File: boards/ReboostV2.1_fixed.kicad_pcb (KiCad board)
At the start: 4 copper layers, 94.5 x 80.5 mm, 184 parts, among them J1 Header 1x4, J2 USB-B-MINI-VERT, J4 TagConnect 6p NL, J8 CAN_BUS-Deutsch_ASL206-05SD-HE, J9 CAN_BUS-Deutsch_ASL206-05SD-HE, Q1 GS61008T, Q2 GS61008T, Q3 MMBT5401LT1G, U10 LP2985AIM5-3.3, U11 TPS7A2501, U1_IHS LTC6362, U1_ILS LTC6362, U2 CP2104-F03-GM, U3 STM32G474, U4 74LVC2G08, U5 Si8273, U6 ISO1044, U7 LM5165XDRCT, U8 LTC3639EMSE, U9 LM5165YDRCT, X1 16MHz

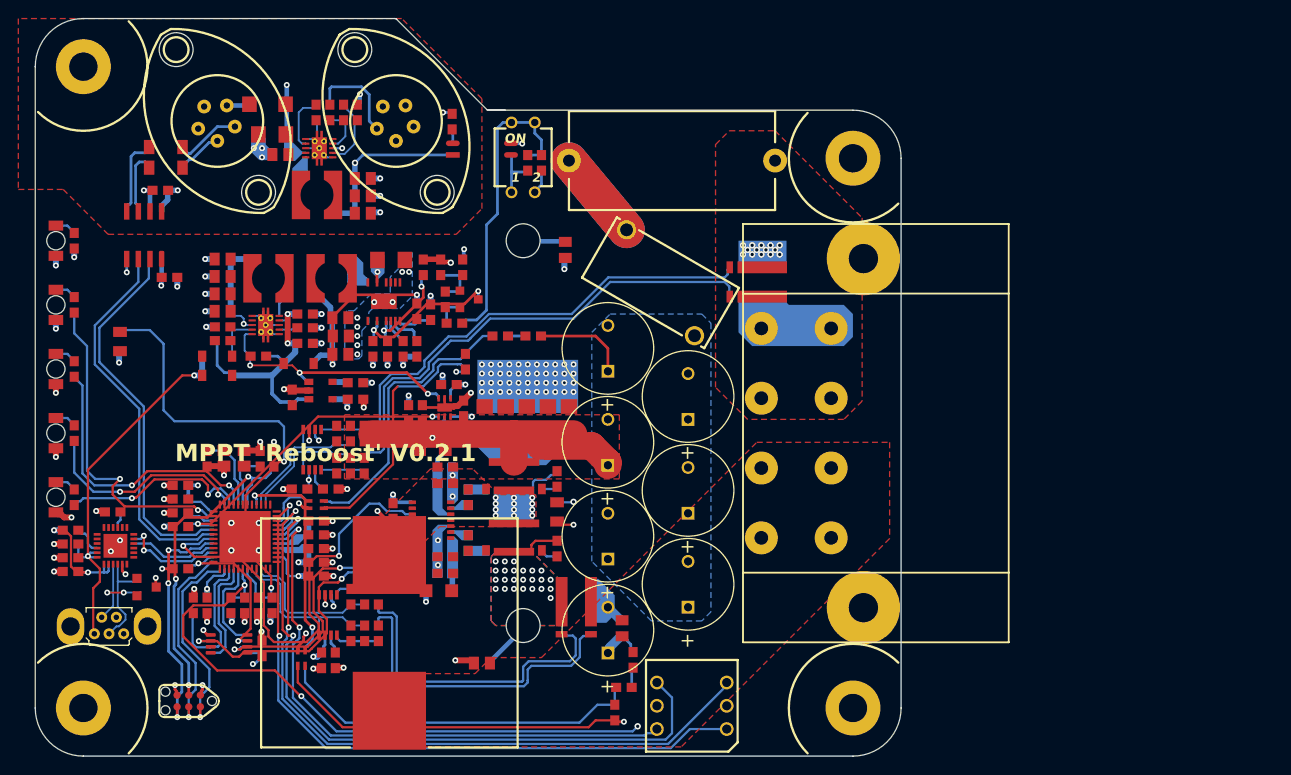
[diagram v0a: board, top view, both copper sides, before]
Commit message: boards: regenerate ReboostV2.1_fixed with faithful relayer (correct full-board layers)
Was the partial-relayer conversion (pads+power on F.Cu, signal traces stranded on
B.Cu, 160/184 footprints on the wrong side). Regenerated with --relayer faithful:
footprints 160 front / 24 back, tracks Top 1184 / Bottom 167 / In2 82 / In1 3 (=
the Altium copper histogram through LMAP), MCU/Q1/Q2 front with pads+traces on
matching layers. 1436 tracks relayered, 184 footprints flipped, 18 zones swapped.
Adds the .altium.json conversion provenance sidecar.
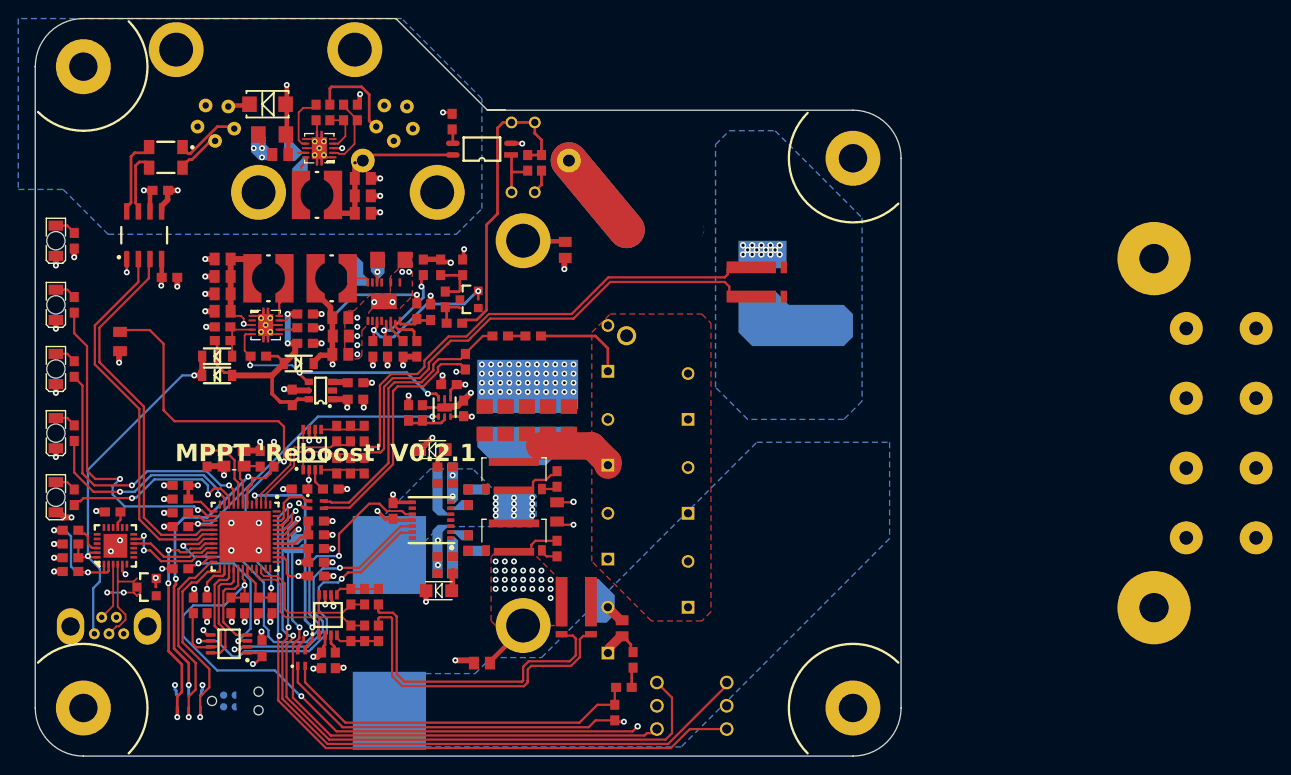
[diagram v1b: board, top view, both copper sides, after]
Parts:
- ? (x7), C22, C23, C24, C25, C26, C28, C34, F1, J1, J2, J4, J8, J9, L1, L2, S1, S2: moved to B.Cu
- C10, C11, C12, C13, C14, C15, C16, C17, C18, C19, C1_IHS, C1_ILS, C20, C21, C27, C29, C2_IHS, C2_ILS, C30, C31, C32, C33, C35, C36, C37, C38, C39, C3_IHS, C3_ILS, C40, C41, C42, C43, C44, C45, C46, C47, C48, C49, C4_IHS, C4_ILS, C5, C50, C51, C52, C53, C54, C55, C56, C57, C58, C59, C6, C60, C61, C62, C64, C65, C66, C67, C7, C8, C9, D1, D2, D3, D4, D5, D6, D7, D8, L3, L4, L5, L6, L7_VHS, L7_VLS, LED1, LED2, LED3, LED4, LED5, MP1, MP2, MP3, MP4, MP5, MP6, Q1, Q2, Q3, R1, R10_IHS, R10_ILS, R11, R12_VHS, R12_VLS, R13_VHS, R13_VLS, R14, R15, R16, R17, R18, R19, R2, R20, R21, R22, R24, R25, R26, R27, R28, R29, R3, R30, R31, R32, R33, R34, R35, R36, R37, R38, R39, R4, R40, R41, R42, R44, R45, R47, R48, R49_VHS, R49_VLS, R5, R50, R53, R6_IHS, R6_ILS, R7_IHS, R7_ILS, R8_IHS, R8_ILS, R9_IHS, R9_ILS, U10, U11, U1_IHS, U1_ILS, U2, U3, U4, U5, U6, U7, U8, U9, X1: moved to F.Cu
- turned ? to 180 degrees (x7)
- turned C12 to 0 degrees
- turned C14 to 0 degrees
- turned C15 to 0 degrees
- turned C17 to 180 degrees
- turned C18 to 0 degrees
- turned C19 to 180 degrees
- turned C27 to 180 degrees
- turned C2_IHS to 180 degrees
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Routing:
- net VLP: track 43.9 -> 4.08 mm, vias 1 -> 0
- net GND: track 125.4 -> 160.7 mm, vias 161 -> 132
- net NetC14_2: track 5.34 -> 32.8 mm, vias 0 -> 5
- net SWO: track 25.6 -> 0.00 mm, vias 3 -> 0
- net Vb: track 87.6 -> 62.6 mm
- net Vdda: track 16.5 -> 29.5 mm, vias 6 -> 10
- net RX: track 9.69 -> 0.00 mm
- net LS: track 10.3 -> 1.06 mm, vias 0 -> 1
- net VDD_CP: track 13.5 -> 19.1 mm, vias 2 -> 4
- net HSS: track 21.6 -> 17.4 mm, vias 15 -> 14
- net NetC27_2: track 5.60 -> 2.20 mm, vias 0 -> 1
- net CGND: track 26.2 -> 22.9 mm, vias 9 -> 3
- net NetR11_1: track 3.33 -> 0.00 mm
- net 5Vcan: track 48.8 -> 51.9 mm, vias 3 -> 6
- net Vusb: track 42.5 -> 44.4 mm, vias 2 -> 4
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- added copper zone on In1.Cu, net CGND
- added copper zone on In1.Cu, net GND
- added copper zone on B.Cu, net HSS
- added copper zone on B.Cu, net SHLD
- added copper zone on B.Cu, net VHP
- added copper zone on In2.Cu, net VHP
- added copper zone on In2.Cu, net VLN
- added copper zone on B.Cu, net VLP
- added copper zone on In2.Cu, net Vdd
- added copper zone on In2.Cu, net Vdda
- removed copper zone on In2.Cu, net CGND
- removed copper zone on B.Cu, net GND
- removed copper zone on In2.Cu, net GND
- removed copper zone on F.Cu, net HSS
- removed copper zone on F.Cu, net SHLD
- removed copper zone on F.Cu, net VHP
- removed copper zone on In1.Cu, net VHP
- removed copper zone on In1.Cu, net VLN
- removed copper zone on F.Cu, net VLP
- removed copper zone on B.Cu, net Vb
- removed copper zone on In1.Cu, net Vdd
- removed copper zone on In1.Cu, net Vdda

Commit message: altium_import: relabel layers instead of mirroring footprints; restore the pour guard
The 'faithful' relayer used fp.Flip(fp.GetPosition(), False) on every footprint.
Flip() MIRRORS each footprint's pad offsets about its own anchor, while tracks
and zones were only layer-swapped, never mirrored -- so pads ended up on copper
they do not touch on the real board. Measured against the raw import, the
committed board had 355 of 544 pads displaced: MLCC terminals exchanged ends by
+-1.7 mm, and Q2's G1/G2 gate pads swapped places by +-6.1 mm.

We are re-interpreting which physical layer each object lives on, not moving
parts to the other side of the board, so the geometry must not move at all.
_relayer_faithful is now a pure layer relabel (pad layer-sets, footprint side
flag, tracks, arcs, blind/buried via spans, zones incl. footprint-owned ones,
and board-level copper shapes). Re-measured: 0 of 541 referenced pads move.

Two things that relabel was still missing, both silent:
  - PCB_ARC copper and board-level gr_* copper shapes were left on the
    un-relabelled layer. ReboostV2 has no arcs but 26 copper shapes -- they
    were stranded on the wrong layer in the committed board.
  - boards with copper beyond In2 were mis-relabelled (only F/B and In1/In2 are
    known); that now raises rather than producing a mixed stack.

The Vb-pour check had been narrowed to `relayer == "partial"`, so 'none',
'groundtruth' and 'faithful' lost BOTH the bridging pour and the warning that
the importer had dropped one. A dropped FET-area Vin pour breaks the loop
whichever relayer ran, so the CHECK is restored for every mode; only the
SYNTHESIS stays partial-only, and the others get a loud warning instead of
invented copper. It fires on the real board: the only surviving Vb zone spans
x=162..175 mm while Q1's Vb pad is at x=153.5 mm.

The check itself was also too weak. It tested a zone BOUNDING-BOX overlap of a
possibly-unfilled zone, so a ring/L-shaped pour elsewhere on the net, or a zon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
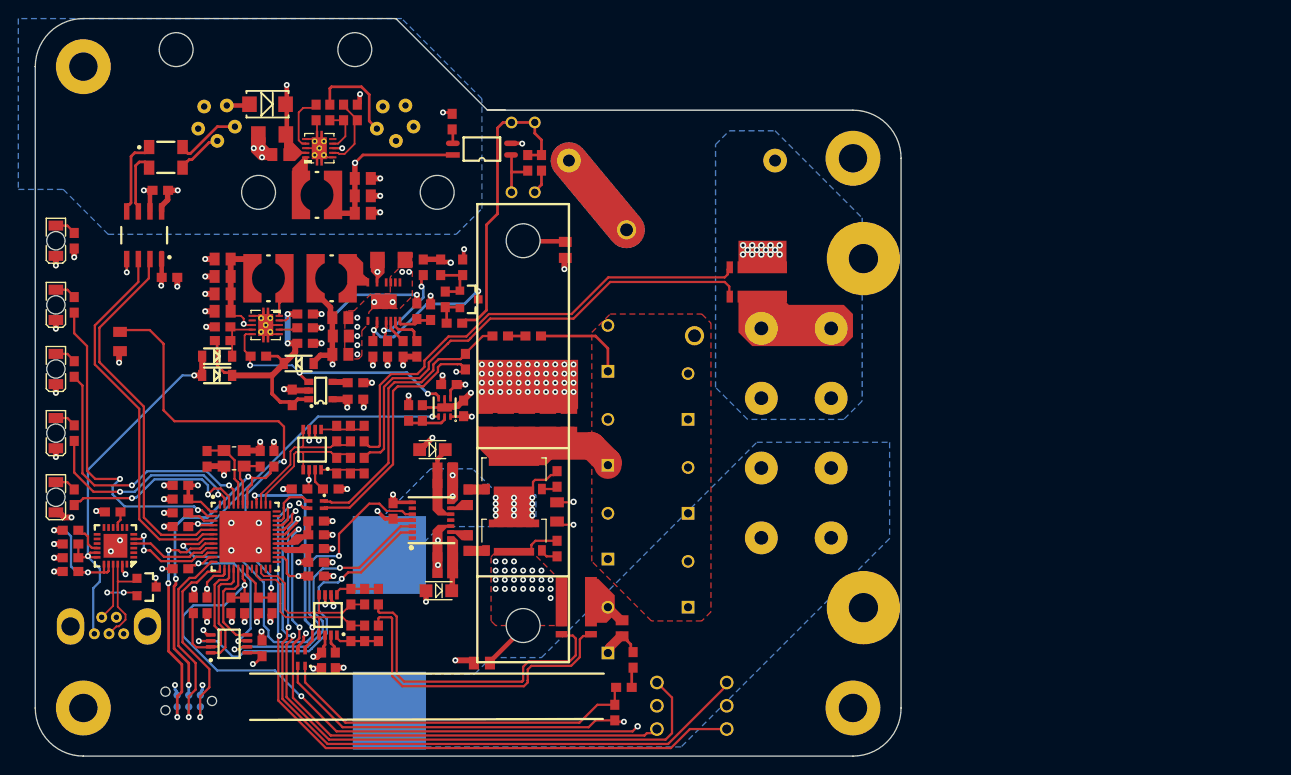
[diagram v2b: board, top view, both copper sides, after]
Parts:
- turned ? to 0 degrees (x7)
- turned C12 to 180 degrees
- turned C14 to 180 degrees
- turned C15 to 180 degrees
- turned C17 to 0 degrees
- turned C18 to 180 degrees
- turned C19 to 0 degrees
- turned C27 to 0 degrees
- turned C2_IHS to 0 degrees
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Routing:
- net NetC14_2: track 32.8 -> 5.34 mm, vias 5 -> 0
- net SWO: track 0.00 -> 25.6 mm, vias 0 -> 3
- net Vdda: track 29.5 -> 16.5 mm, vias 10 -> 6
- net GND: track 160.7 -> 170.7 mm, vias 132 -> 164
- net RX: track 0.00 -> 9.69 mm
- net LS: track 1.06 -> 10.3 mm, vias 1 -> 0
- net VDD_CP: track 19.1 -> 13.5 mm, vias 4 -> 2
- net NetC27_2: track 2.20 -> 5.60 mm, vias 1 -> 0
- net CGND: track 22.9 -> 26.2 mm, vias 3 -> 9
- net NetR11_1: track 0.00 -> 3.33 mm
- net 5Vcan: track 51.9 -> 48.8 mm, vias 6 -> 3
- net VLS: track 26.1 -> 23.9 mm, vias 3 -> 2
- net Vusb: track 44.4 -> 42.5 mm, vias 4 -> 2
- net Vdds: track 31.5 -> 29.6 mm, vias 4 -> 2
- net NetL3_1: track 0.00 -> 1.45 mm
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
